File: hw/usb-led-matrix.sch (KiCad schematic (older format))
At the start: 102 parts, among them J1 USB4085-GF-A, J2 Conn_ST_STDC14, U1 AP2210K-3.3, U2 STM32G473CET6, U3 74LVT245, U4 USBLC6-2SC6, Y1 ABM8-24.000MHZ-B2-T

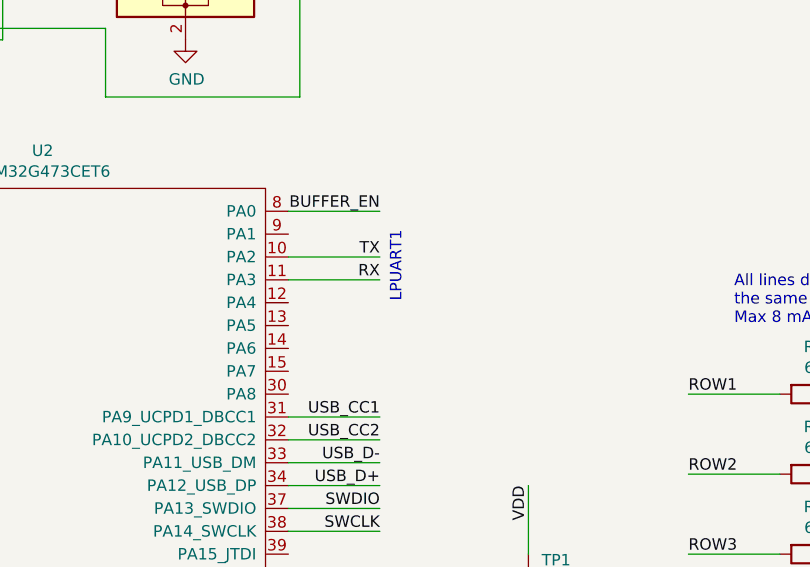
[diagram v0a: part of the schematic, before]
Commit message: Fine tune PCB, silkscreen rev.A
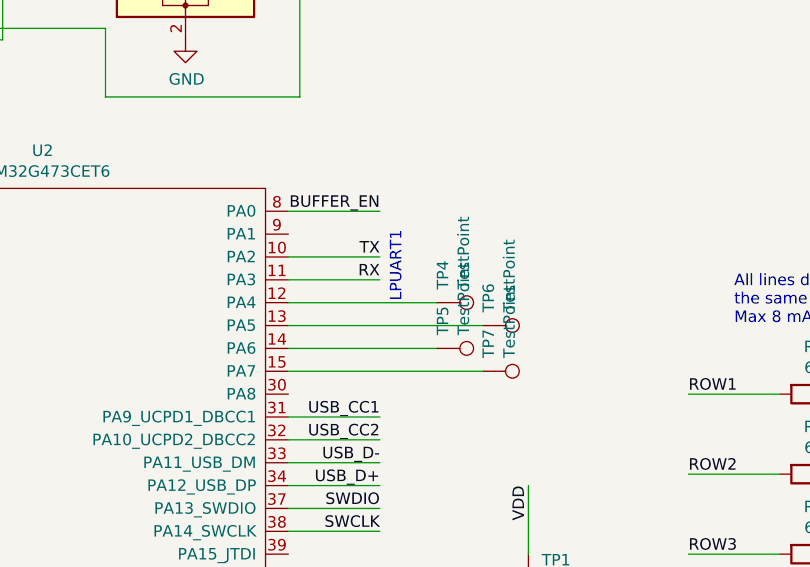
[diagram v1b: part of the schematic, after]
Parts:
- added TP4, TP5, TP6, TP7: TestPoint, TestPoint:TestPoint_Pad_1.0x1.0mm, symbol Connector:TestPoint
- Y1: footprint Crystal:Crystal_SMD_3225-4Pin_3.2x2.5mm -> jonas_Crystal:Crystal_SMD_3225-4Pin_3.2x2.5mm
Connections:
- net at U2.12 (PA4): now also TP4.1
- net at U2.13 (PA5): now also TP6.1
- net at U2.14 (PA6): now also TP5.1
- net at U2.15 (PA7): now also TP7.1
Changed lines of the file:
@@
 F 0 "Y1" V 2704 5994 50  0000 L CNN
 F 1 "ABM8-24.000MHZ-B2-T" V 2795 5994 50  0000 L CNN
-F 2 "Crystal:Crystal_SMD_3225-4Pin_3.2x2.5mm" H 2750 5750 50  0001 C CNN
+F 2 "jonas_Crystal:Crystal_SMD_3225-4Pin_3.2x2.5mm" H 2750 5750 50  0001 C CNN
 F 3 "~" H 2750 5750 50  0001 C CNN
 	1    2750 5750
@@
 Wire Wire Line
 	9100 950  9100 1850
+$Comp
+L Connector:TestPoint TP4
+U 1 1 5FF8A342
+P 6550 3250
+F 0 "TP4" H 6492 3276 50  0000 R CNN
+F 1 "TestPoint" H 6492 3367 50  0000 R CNN
+F 2 "TestPoint:TestPoint_Pad_1.0x1.0mm" H 6750 3250 50  0001 C CNN
+F 3 "~" H 6750 3250 50  0001 C CNN
+	1    6550 3250
+	0    1    1    0
+$EndComp
+$Comp
+L Connector:TestPoint TP6
+U 1 1 5FF8AC19
+P 6750 3350
+F 0 "TP6" H 6692 3376 50  0000 R CNN
+F 1 "TestPoint" H 6692 3467 50  0000 R CNN
+F 2 "TestPoint:TestPoint_Pad_1.0x1.0mm" H 6950 3350 50  0001 C CNN
+F 3 "~" H 6950 3350 50  0001 C CNN
+	1    6750 3350
+	0    1    1    0
+$EndComp
+$Comp
+L Connector:TestPoint TP5
+U 1 1 5FF8AFDB
+P 6550 3450
+F 0 "TP5" H 6492 3476 50  0000 R CNN
+F 1 "TestPoint" H 6492 3567 50  0000 R CNN
+F 2 "TestPoint:TestPoint_Pad_1.0x1.0mm" H 6750 3450 50  0001 C CNN
+F 3 "~" H 6750 3450 50  0001 C CNN
+	1    6550 3450
+	0    1    1    0
+$EndComp
+$Comp
+L Connector:TestPoint TP7
+U 1 1 5FF8B267
+P 6750 3550
+F 0 "TP7" H 6692 3576 50  0000 R CNN
+F 1 "TestPoint" H 6692 3667 50  0000 R CNN
+F 2 "TestPoint:TestPoint_Pad_1.0x1.0mm" H 6950 3550 50  0001 C CNN
+F 3 "~" H 6950 3550 50  0001 C CNN
+	1    6750 3550
+	0    1    1    0
+$EndComp
+Wire Wire Line
+	5900 3250 6550 3250
+Wire Wire Line
+	5900 3450 6550 3450
+Wire Wire Line
+	5900 3350 6750 3350
+Wire Wire Line
+	5900 3550 6750 3550
 $EndSCHEMATC
